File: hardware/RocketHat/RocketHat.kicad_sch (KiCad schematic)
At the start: 2 parts, among them J1 Conn_02x16_Top_Bottom, J2 Conn_02x16_Top_Bottom

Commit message: Rocket hat sensor libraries
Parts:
- added U1: BMP390, bmp390:10LGA_2X2X0p75_BOS, symbol BMP390:BMP390
- added U2: BMI088, Package_LGA:Bosch_LGA-16_4.5x3mm_P0.5mm_LayoutBorder7x1y_ClockwisePinNumbering, symbol Sensor_Motion:BMI088
- added U3: ADXL375BCCZ, adxl375:LGA_CC-14-1_ADI, symbol ADXL375:ADXL375BCCZ
- added U4: CAM-M8C-0, CAM-M8C-0:CAM-M8C-0, symbol CAM-M8C-0:CAM-M8C-0
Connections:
- new net: U2.2 (GNDA), U2.4 (GNDA)

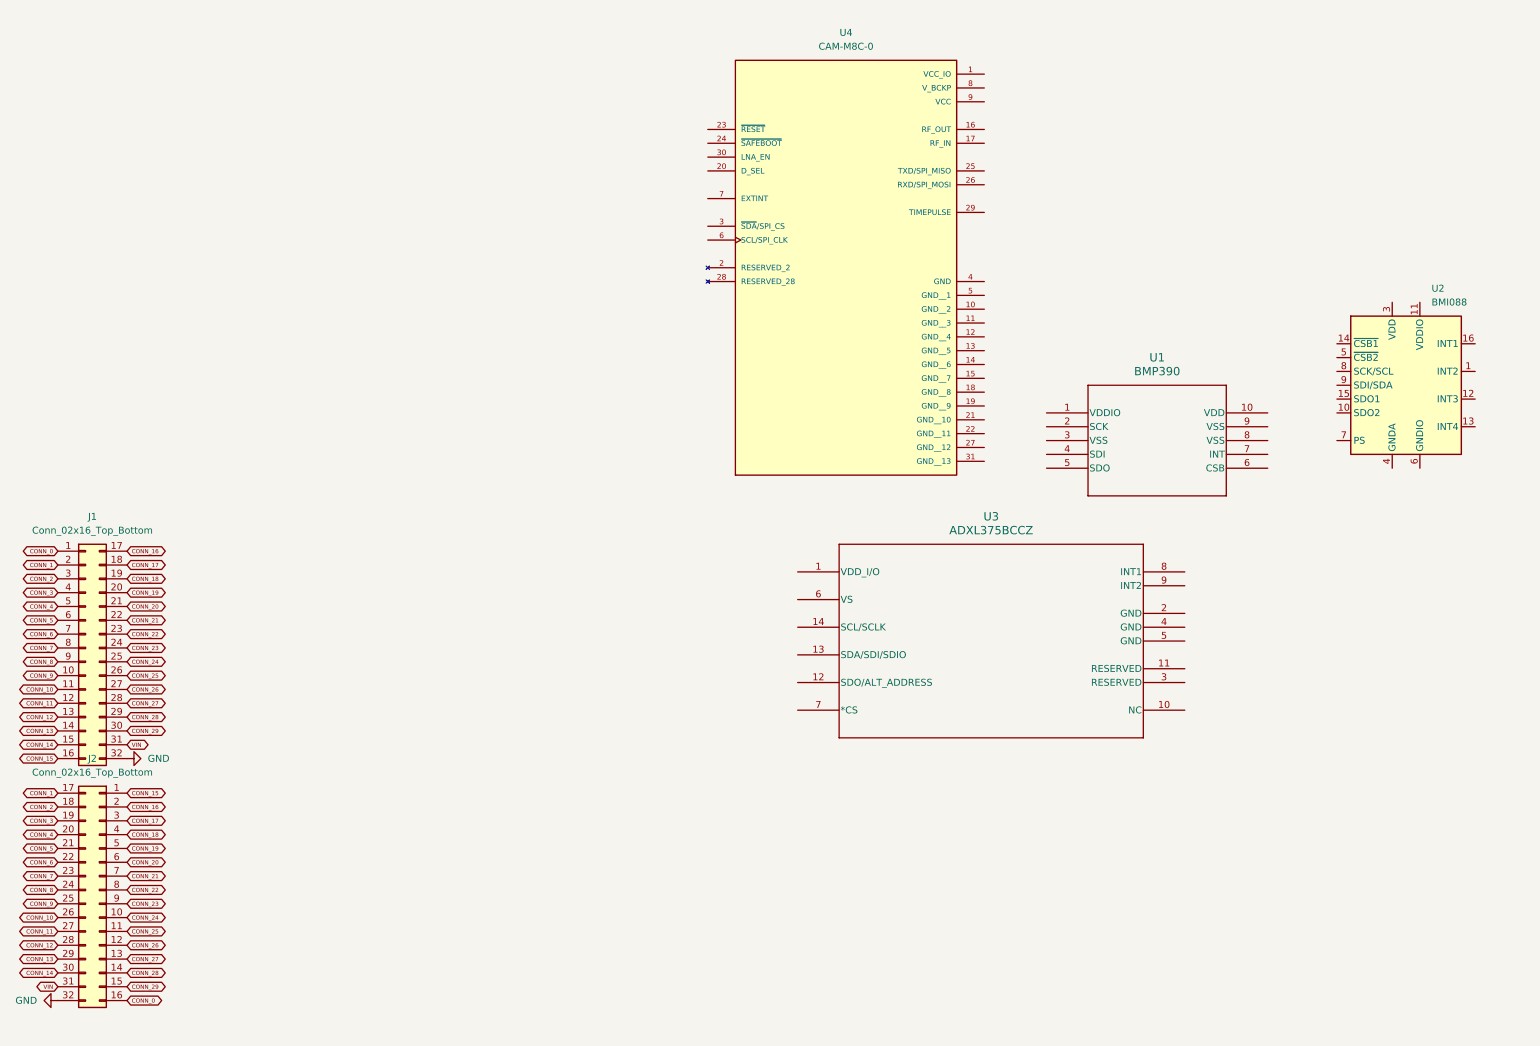
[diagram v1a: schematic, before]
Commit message: Rocket Hat schematic done
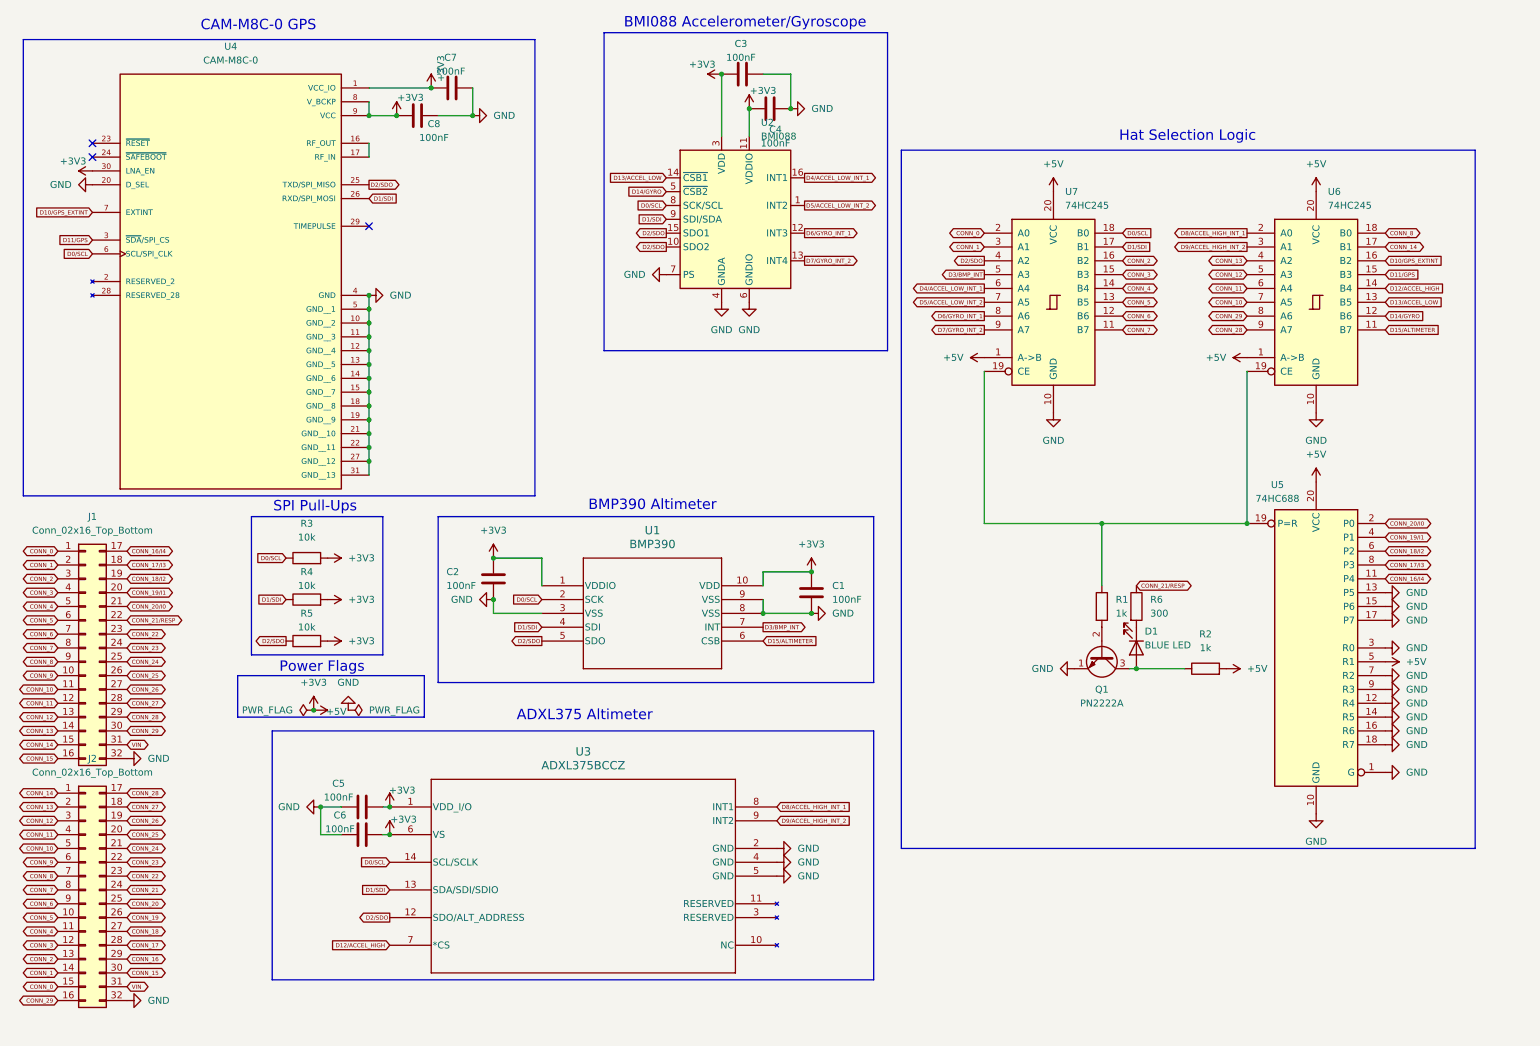
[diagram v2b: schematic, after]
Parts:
- removed U2: BMI088, Package_LGA:Bosch_LGA-16_4.5x3mm_P0.5mm_LayoutBorder7x1y_ClockwisePinNumbering, symbol Sensor_Motion:BMI088
- added C1, C2, C3, C4, C5, C6, C7, C8: 100nF, symbol Device:C
- added D1: BLUE LED, symbol Device:LED
- added Q1: PN2222A, Package_TO_SOT_THT:TO-92_Inline, symbol Transistor_BJT:PN2222A
- added R1, R2: 1k, symbol Device:R
- added R3, R4, R5: 10k, symbol Device:R
- added R6: 300, symbol Device:R
- added U2: BMI088, Package_LGA:Bosch_LGA-16_4.5x3mm_P0.5mm_LayoutBorder7x1y_ClockwisePinNumbering, symbol BMI088:BMI088
- added U5: 74HC688, symbol 74xx:74HC688
- added U6, U7: 74HC245, symbol 74xx:74HC245
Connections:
- net CONN_0: now also J2.15 (Pin_15), U7.2 (A0); no longer J2.16 (Pin_16)
- net CONN_1: now also J2.14 (Pin_14), U7.3 (A1); no longer J2.17 (Pin_17)
- net CONN_10: now also J2.5 (Pin_5), U6.7 (A5); no longer J2.26 (Pin_26)
- net CONN_11: now also J2.4 (Pin_4), U6.6 (A4); no longer J2.27 (Pin_27)
- net CONN_12: now also J2.3 (Pin_3), U6.5 (A3); no longer J2.28 (Pin_28)
- net CONN_13: now also J2.2 (Pin_2), U6.4 (A2); no longer J2.29 (Pin_29)
- net CONN_14: now also J2.1 (Pin_1), U6.17 (B1); no longer J2.30 (Pin_30)
- net CONN_15: now also J2.30 (Pin_30); no longer J2.1 (Pin_1)
- net CONN_16: now also J2.29 (Pin_29); no longer J1.17 (Pin_17), J2.2 (Pin_2)
- net CONN_17: now also J2.28 (Pin_28); no longer J1.18 (Pin_18), J2.3 (Pin_3)
- net CONN_18: now also J2.27 (Pin_27); no longer J1.19 (Pin_19), J2.4 (Pin_4)
- net CONN_19: now also J2.26 (Pin_26); no longer J1.20 (Pin_20), J2.5 (Pin_5)
- net CONN_2: now also J2.13 (Pin_13), U7.16 (B2); no longer J2.18 (Pin_18)
- net CONN_20: now also J2.25 (Pin_25); no longer J1.21 (Pin_21), J2.6 (Pin_6)
- net CONN_21: now also J2.24 (Pin_24); no longer J1.22 (Pin_22), J2.7 (Pin_7)
- net CONN_22: now also J2.23 (Pin_23); no longer J2.8 (Pin_8)
- net CONN_23: now also J2.22 (Pin_22); no longer J2.9 (Pin_9)
- net CONN_24: now also J2.21 (Pin_21); no longer J2.10 (Pin_10)
- net CONN_25: now also J2.20 (Pin_20); no longer J2.11 (Pin_11)
- net CONN_26: now also J2.19 (Pin_19); no longer J2.12 (Pin_12)
- net CONN_27: now also J2.18 (Pin_18); no longer J2.13 (Pin_13)
- net CONN_28: now also J2.17 (Pin_17), U6.9 (A7); no longer J2.14 (Pin_14)
- net CONN_29: now also J2.16 (Pin_16), U6.8 (A6); no longer J2.15 (Pin_15)
- net CONN_3: now also J2.12 (Pin_12), U7.15 (B3); no longer J2.19 (Pin_19)
- net CONN_4: now also J2.11 (Pin_11), U7.14 (B4); no longer J2.20 (Pin_20)
- net CONN_5: now also J2.10 (Pin_10), U7.13 (B5); no longer J2.21 (Pin_21)
- net CONN_6: now also J2.9 (Pin_9), U7.12 (B6); no longer J2.22 (Pin_22)
- net CONN_7: now also J2.8 (Pin_8), U7.11 (B7); no longer J2.23 (Pin_23)
- net CONN_8: now also J2.7 (Pin_7), U6.18 (B0); no longer J2.24 (Pin_24)
- net CONN_9: now also J2.6 (Pin_6); no longer J2.25 (Pin_25)
- net GND: now also U1.3 (VSS), U1.8 (VSS), U1.9 (VSS), U3.2 (GND), U3.4 (GND), U3.5 (GND), U4.10 (GND__2), U4.11 (GND__3), U4.12 (GND__4), U4.13 (GND__5), U4.14 (GND__6), U4.15 (GND__7), U4.18 (GND__8), U4.19 (GND__9), U4.20 (D_SEL), U4.21 (GND__10), U4.22 (GND__11), U4.27 (GND__12), U4.31 (GND__13), U4.4 (GND), U4.5 (GND__1), C1.2, C2.2, C3.1, C4.1, C5.2, C6.2, C7.1, C8.1, Q1.1 (E), U2.2 (GNDA), U2.4 (GNDA), U2.6 (GNDIO), U2.7 (PS), U5.1 (G), U5.10 (GND), U5.12 (R4), U5.13 (P5), U5.14 (R5), U5.15 (P6), U5.16 (R6), U5.17 (P7), U5.18 (R7), U5.3 (R0), U5.7 (R2), U5.9 (R3), U6.10 (GND), U7.10 (GND)
- net +3V3: now reaches U1.1 (VDDIO)
- net +3V3: now also U1.10 (VDD), U3.1 (VDD_I/O), U3.6 (VS), U4.1 (VCC_IO), U4.30 (LNA_EN), U4.8 (V_BCKP), U4.9 (VCC), C1.1, C2.1, C3.2, C4.2, C5.1, C6.1, C7.2, C8.2, R2.2, R3.2, R4.2, R5.2, U2.11 (VDDIO), U2.3 (VDD), U5.20 (VCC), U5.5 (R1), U6.1 (A->B), U6.20 (VCC), U7.1 (A->B), U7.20 (VCC)
- net D0/SCL: now reaches U1.2 (SCK)
- net D0/SCL: now also U3.14 (SCL/SCLK), U4.6 (SCL/SPI_CLK), R3.1, U2.8 (SCK/SCL), U7.18 (B0)
- net D1/SDI: now reaches U1.4 (SDI)
- net D1/SDI: now also U3.13 (SDA/SDI/SDIO), U4.26 (RXD/SPI_MOSI), R4.1, U2.9 (SDI/SDA), U7.17 (B1)
- net D2/SDO: now reaches U1.5 (SDO)
- net D2/SDO: now also U3.12 (SDO/ALT_ADDRESS), U4.25 (TXD/SPI_MISO), R5.1, U2.10 (SDO2), U2.15 (SDO1), U7.4 (A2)
- net D15/ALTIMETER: now reaches U1.6 (CSB)
- net D15/ALTIMETER: now also U6.11 (B7)
- net D3/BMP_INT: now reaches U1.7 (INT)
- net D3/BMP_INT: now also U7.5 (A3)
- net D12/ACCEL_HIGH: now reaches U3.7 (*CS)
- net D12/ACCEL_HIGH: now also U6.14 (B4)
- net D8/ACCEL_HIGH_INT_1: now reaches U3.8 (INT1)
- net D8/ACCEL_HIGH_INT_1: now also U6.2 (A0)
- net D9/ACCEL_HIGH_INT_2: now reaches U3.9 (INT2)
- net D9/ACCEL_HIGH_INT_2: now also U6.3 (A1)
- net at U4.16 (RF_OUT): now also U4.17 (RF_IN)
- net D11/GPS: now reaches U4.3 (~{SDA}/SPI_CS)
- net D11/GPS: now also U6.15 (B3)
- net D10/GPS_EXTINT: now reaches U4.7 (EXTINT)
- net D10/GPS_EXTINT: now also U6.16 (B2)
- new net: R1.1, U5.19 (P=R), U6.19 (CE), U7.19 (CE)
- new net: D1.1 (K), R6.2
- new net: D1.2 (A), Q1.3 (C), R2.1
- new net: Q1.2 (B), R1.2
- new net CONN_16/I4: J1.17 (Pin_17), U5.11 (P4)
- new net CONN_17/I3: J1.18 (Pin_18), U5.8 (P3)
- new net CONN_18/I2: J1.19 (Pin_19), U5.6 (P2)
- new net CONN_19/I1: J1.20 (Pin_20), U5.4 (P1)
- new net CONN_20/I0: J1.21 (Pin_21), U5.2 (P0)
- new net CONN_21/RESP: J1.22 (Pin_22), R6.1
- new net D13/ACCEL_LOW: U2.14 (~{CSB1}), U6.13 (B5)
- new net D14/GYRO: U2.5 (~{CSB2}), U6.12 (B6)
- new net D4/ACCEL_LOW_INT_1: U2.16 (INT1), U7.6 (A4)
- new net D5/ACCEL_LOW_INT_2: U2.1 (INT2), U7.7 (A5)
- new net D6/GYRO_INT_1: U2.12 (INT3), U7.8 (A6)
- new net D7/GYRO_INT_2: U2.13 (INT4), U7.9 (A7)
- no-connect marks 0 -> 3
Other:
- note added: "ADXL375 Altimeter"
- note added: "BMI088 Accelerometer/Gyroscope"
- note added: "BMP390 Altimeter"
- note added: "CAM-M8C-0 GPS"
- note added: "Hat Selection Logic"
- note added: "Power Flags"
- note added: "SPI Pull-Ups"
- company: (none) -> UNR Aerospace Club
- title: T.A.C.O.S -> T.A.C.O.S Rocket Hat

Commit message: rocket hat footprints done
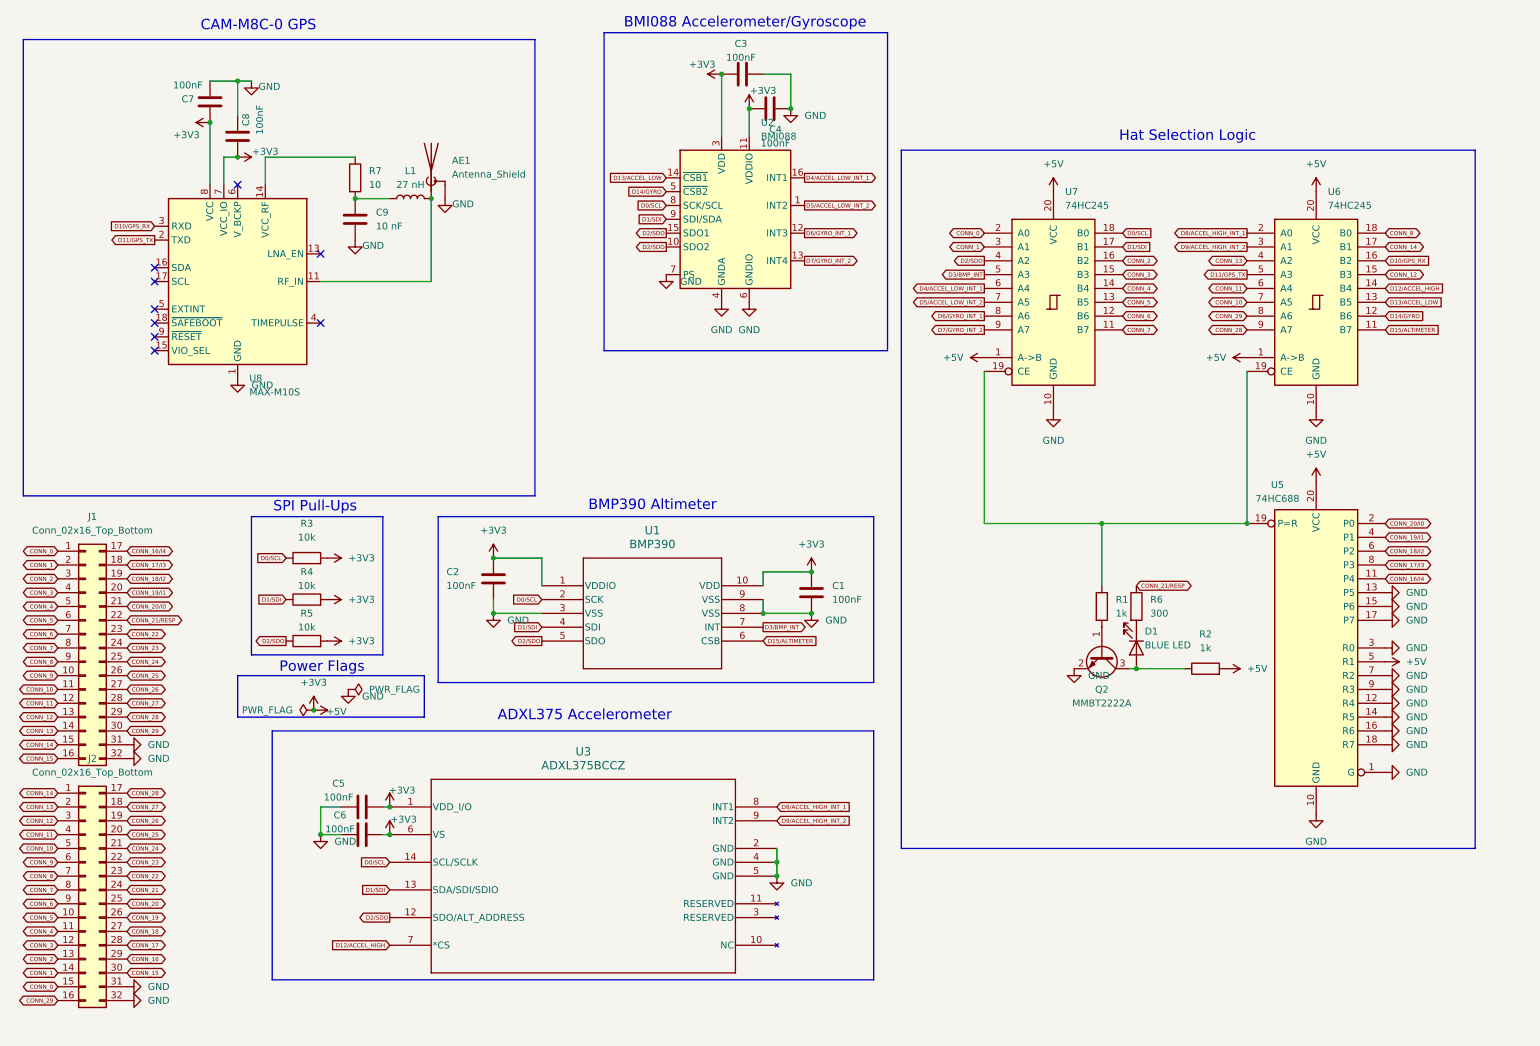
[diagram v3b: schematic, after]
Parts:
- removed Q1: PN2222A, Package_TO_SOT_THT:TO-92_Inline, symbol Transistor_BJT:PN2222A
- removed U4: CAM-M8C-0, CAM-M8C-0:CAM-M8C-0, symbol CAM-M8C-0:CAM-M8C-0
- added AE1: Antenna_Shield, Connector_Coaxial:U.FL_Molex_MCRF_73412-0110_Vertical, symbol Device:Antenna_Shield
- added C9: 10 nF, Capacitor_SMD:C_0201_0603Metric, symbol Device:C
- added L1: 27 nH, Inductor_SMD:L_0201_0603Metric, symbol Device:L
- added Q2: MMBT2222A, Package_TO_SOT_SMD:SOT-23, symbol Transistor_BJT:MMBT2222A
- added R7: 10, Resistor_SMD:R_0201_0603Metric, symbol Device:R
- added U8: MAX-M10S, RF_GPS:ublox_MAX, symbol RF_GPS:MAX-M10S
- C1, C2, C3, C4, C5, C6, C7, C8: footprint (none) -> Capacitor_SMD:C_0201_0603Metric
- D1: footprint (none) -> LED_SMD:LED_0201_0603Metric
- R1, R2, R3, R4, R5, R6: footprint (none) -> Resistor_SMD:R_0201_0603Metric
- U5: footprint (none) -> Package_SO:TSSOP-20_4.4x6.5mm_P0.65mm
- U6, U7: footprint (none) -> Package_DFN_QFN:DHVQFN-20-1EP_2.5x4.5mm_P0.5mm_EP1x3mm
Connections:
- net D11/GPS is gone; now on net CONN_12: U6.15 (B3)
- net VIN is gone; now on net GND: J1.31 (Pin_31), J2.31 (Pin_31)
- net +3V3: now also U8.7 (VCC_IO), U8.8 (VCC)
- net CONN_12: no longer U6.5 (A3)
- net GND: now also AE1.2 (Shield), C9.2, Q2.2 (E), U8.1 (GND), U8.10 (GND), U8.12 (GND)
- net at D1.2 (A), R2.1: now also Q2.3 (C)
- net at R1.2: now also Q2.1 (B)
- net D10/GPS_EXTINT renamed D10/GPS_RX
- net D10/GPS_RX: now also U8.3 (RXD)
- new net: C9.1, L1.1, R7.2
- new net: AE1.1 (A), L1.2, U8.11 (RF_IN)
- new net: R7.1, U8.14 (VCC_RF)
- new net D11/GPS_TX: U6.5 (A3), U8.2 (TXD)
- no-connect marks 3 -> 9
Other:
- note added: "ADXL375 Accelerometer"
- note removed: "ADXL375 Altimeter"
- moved on the sheet: C7, C8

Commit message: rocket hat connector labels
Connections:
- net CONN_20 is gone; now on net +3V3: J2.25 (Pin_25)
- net CONN_21 is gone; now on net +3V3: J2.24 (Pin_24)
- net CONN_22 is gone; now on net +3V3: J1.23 (Pin_23), J2.23 (Pin_23)
- net CONN_24 is gone; now on net +5V: J1.25 (Pin_25), J2.21 (Pin_21)
- net CONN_25 is gone; now on net +5V: J1.26 (Pin_26), J2.20 (Pin_20)
- net CONN_26 is gone; now on net GND: J1.27 (Pin_27), J2.19 (Pin_19)
- net CONN_27 is gone; now on net GND: J1.28 (Pin_28), J2.18 (Pin_18)
- net CONN_9 is gone; now on net CONN_9/RESP: J1.10 (Pin_10), J2.6 (Pin_6)
- net +3V3: now also J1.21 (Pin_21), J1.22 (Pin_22); no longer R2.2, U5.20 (VCC), U5.5 (R1), U6.1 (A->B), U6.20 (VCC), U7.1 (A->B), U7.20 (VCC)
- net CONN_0 renamed CONN_0/D0
- net CONN_1 renamed CONN_1/D1
- net CONN_10 renamed CONN_10/D13
- net CONN_11 renamed CONN_11/D12
- net CONN_12 renamed CONN_12/D11
- net CONN_13 renamed CONN_13/D10
- net CONN_14 renamed CONN_14/D9
- net CONN_15 renamed CONN_15/I4
- net CONN_15/I4: now also U5.11 (P4)
- net CONN_16 renamed CONN_16/I3
- net CONN_16/I3: now also J1.17 (Pin_17), U5.8 (P3)
- removed net CONN_16/I4: J1.17 (Pin_17), U5.11 (P4)
- net CONN_17 renamed CONN_17/I2
- net CONN_17/I2: now also J1.18 (Pin_18), U5.6 (P2)
- removed net CONN_17/I3: J1.18 (Pin_18), U5.8 (P3)
- net CONN_18 renamed CONN_18/I1
- net CONN_18/I1: now also J1.19 (Pin_19), U5.4 (P1)
- removed net CONN_18/I2: J1.19 (Pin_19), U5.6 (P2)
- net CONN_19 renamed CONN_19/I0
- net CONN_19/I0: now also J1.20 (Pin_20), U5.2 (P0)
- removed net CONN_19/I1: J1.20 (Pin_20), U5.4 (P1)
- net CONN_2 renamed CONN_2/D2
- removed net CONN_20/I0: J1.21 (Pin_21), U5.2 (P0)
- net CONN_21/RESP renamed CONN_9/RESP
- net CONN_9/RESP: no longer J1.22 (Pin_22)
- net CONN_23 renamed +5V
- net +5V: now also R2.2, U5.20 (VCC), U5.5 (R1), U6.1 (A->B), U6.20 (VCC), U7.1 (A->B), U7.20 (VCC)
- net CONN_28 renamed CONN_28/D15
- net CONN_29 renamed CONN_29/D14
- net CONN_3 renamed CONN_3/D3
- net CONN_4 renamed CONN_4/D4
- net CONN_5 renamed CONN_5/D5
- net CONN_6 renamed CONN_6/D6
- net CONN_7 renamed CONN_7/D7
- net CONN_8 renamed CONN_8/D8
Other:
- moved on the sheet: J1, J2
